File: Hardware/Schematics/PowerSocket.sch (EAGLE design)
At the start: 30 parts, among them IC1 ACS712-LC, T1 BT138-V, T2 BT138-V

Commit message: Updated schematic to use for a 3 slot device.
Some routing still remaining.
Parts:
- removed U$1: HLK-PM03, PowerSocket:HLK-PM03
- added ACOUT-NULL1, ACOUT-NULL2, ACOUT-PHASE1, ACOUT-PHASE2: -, wirepad:3,81/1,4
- added BUTTON_LED+1, BUTTON_LED+2, BUTTON_LED-1, BUTTON_LED-2, BUTTON_SWITCH3, BUTTON_SWITCH4, BUTTON_SWITCH5, BUTTON_SWITCH6: -, wirepad:2,15/1,0
- added C5, C7: 100nF, rcl:C-EUC1206
- added C6, C8: 470nF, rcl:C-EUC1206
- added D1: 1N4004, diode:1N4004
- added IC2, IC3: ACS712-LC, allegro-2:ACS712-LC
- added OK3, OK4, OK5, OK6: MOC3041S, optocoupler:MOC3041S
- added R11: 10K, rcl:R-TRIMM3296W
- added R12, R13, R14, R15, R16, R17, R18, R19: 150, eagle-ltspice:RR2010
- added R20, R22: 100, eagle-ltspice:RR2010
- added R21, R23: 10K, eagle-ltspice:RR2010
- added R5: 0, eagle-ltspice:RR2010
- added R6: 1M, rcl:R-TRIMM3296W
- added SUPPLY_3.3: 3.3V, wirepad:2,15/1,0
- added SUPPLY_GND: GND, wirepad:2,15/1,0
- added T3, T4, T5, T6: BT138-V, triac:BT138-V
- C3: device rcl:C-EUC1210 -> rcl:C-EU025-024X044
- OK1, OK2: value MOC3041M -> MOC3041S; device optocoupler:MOC3041M -> optocoupler:MOC3041S
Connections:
- removed net N$9 (its old number): ACIN-PHASE.P, T2.A1, U$1.AC1
- new net N$14: ACOUT-NULL1.P, R13.2, T3.A2
- new net N$16: BUTTON_LED+1.P, R20.2
- new net N$24: D1.A, R6.S
- new net N$25: R12.1, R14.2, U$2.IO12
- new net N$26: C6.2, IC2.FILTER
- new net N$27: IC2.VOUT, U$2.IO35
- new net N$28: OK3.C, R12.2
- new net N$29: OK3.A2, R13.1
- new net N$3: R11.S, R6.E, U$2.IO26
- new net N$30: OK3.A1, T3.G
- new net N$31: BUTTON_LED-1.P, U$2.IO23
- new net N$32: OK4.C, R14.1
- new net N$33: OK4.A2, R15.1
- new net N$34: OK4.A1, T4.G
- new net N$35: IC2.IP+, IC2.IP+1, R15.2, T4.A2
- new net N$36: ACOUT-PHASE1.P, IC2.IP-, IC2.IP-1
- new net N$37: BUTTON_LED+2.P, R22.2
- new net N$38: ACOUT-NULL2.P, R17.2, T5.A2
- new net N$39: BUTTON_SWITCH5.P, R23.2, U$2.IO17
- new net N$40: C8.2, IC3.FILTER
- new net N$41: IC3.VOUT, U$2.IO32
- new net N$42: OK5.C, R16.2
- new net N$43: OK5.A2, R17.1
- new net N$44: OK5.A1, T5.G
- new net N$45: ACIN-NULL.P, R5.1, T1.A1, T3.A1, T5.A1
- new net N$46: OK6.C, R18.1
- new net N$47: OK6.A2, R19.1
- new net N$48: OK6.A1, T6.G
- new net N$49: IC3.IP+, IC3.IP+1, R19.2, T6.A2
- new net N$50: ACOUT-PHASE2.P, IC3.IP-, IC3.IP-1
- new net N$51: ACIN-PHASE.P, D1.C, T2.A1, T4.A1, T6.A1
- new net N$52: BUTTON_LED-2.P, U$2.IO5
- new net N$54: R16.1, R18.2, U$2.IO14
- net GND: now also C5.2, C6.1, C7.2, C8.1, IC2.GND, IC3.GND, R11.E, R21.1, R23.1, R5.2, SUPPLY_GND.P; no longer U$1.-VO
- net N$17: now also U$2.IO19; no longer U$2.IO23
- net N$20: now also BUTTON_SWITCH3.P, R21.2, U$2.IO18; no longer ACIN-NULL.P, T1.A1, U$1.AC2
- net N$8: now also U$2.IO13; no longer U$2.IO17
- net VCC: now also BUTTON_SWITCH4.P, BUTTON_SWITCH6.P, C5.1, C7.1, IC2.VCC, IC3.VCC, OK3.A, OK4.A, OK5.A, OK6.A, R20.1, R22.1, SUPPLY_3.3.P; no longer U$1.+VO
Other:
- moved on the sheet: ACOUT-NULL, BUTTON_LED+, BUTTON_LED-, BUTTON_SWITCH1, BUTTON_SWITCH2, OK1, R3, R4, R7, R8, T1

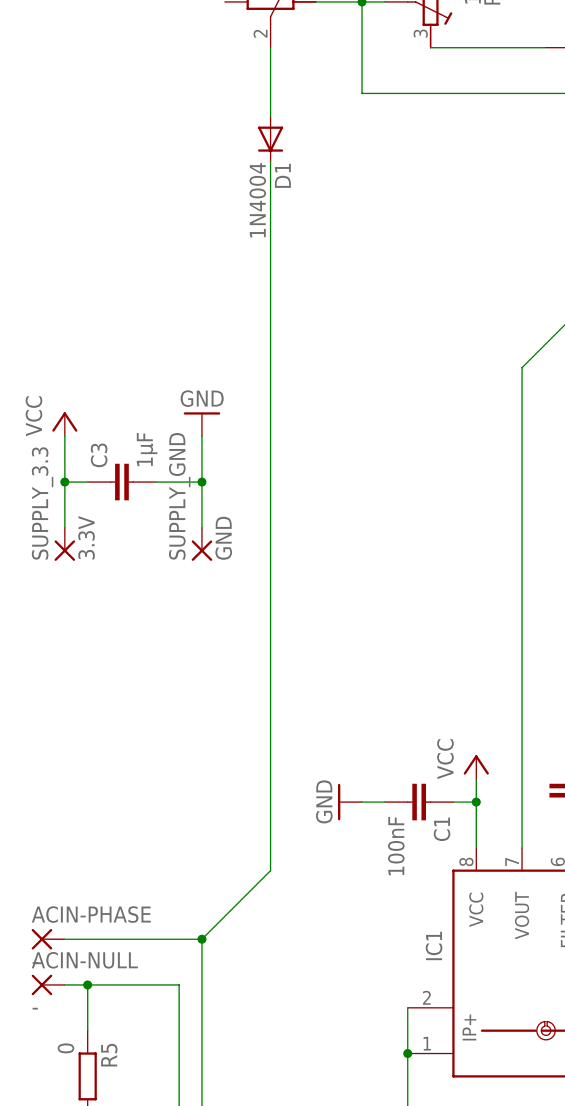
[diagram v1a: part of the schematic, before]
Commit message: Changed dimension to 50mmx100mm and routed the board
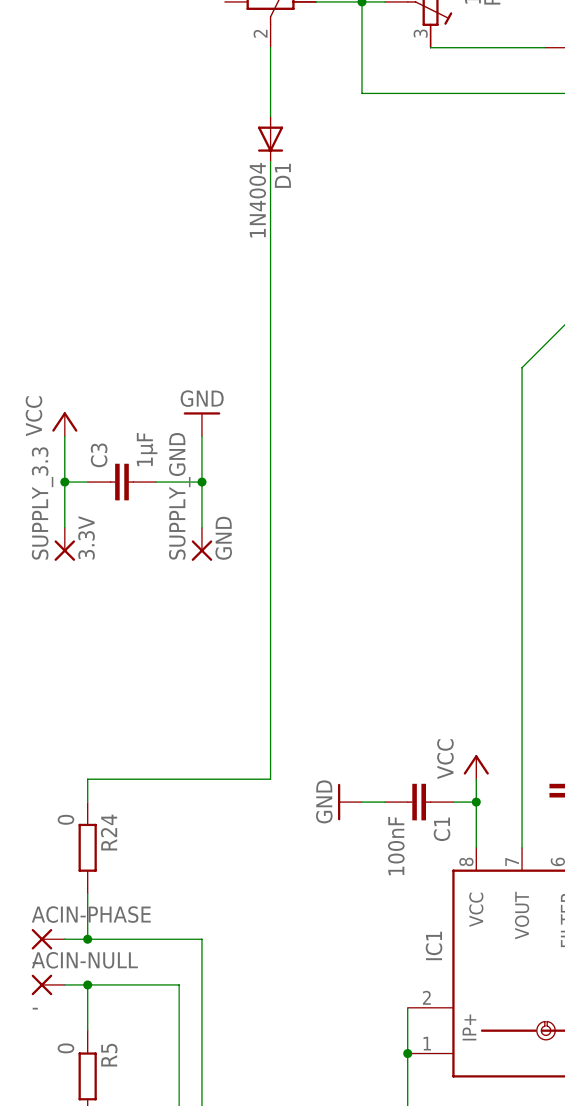
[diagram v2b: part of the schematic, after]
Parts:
- added R24: 0, eagle-ltspice:RR2010
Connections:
- new net N$53: D1.C, R24.1
- net N$51: now also R24.2; no longer D1.C
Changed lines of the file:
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@@
 <?xml version="1.0" encoding="utf-8"?>
 <!DOCTYPE eagle SYSTEM "eagle.dtd">
-<eagle version="7.6.0">
+<eagle version="6.6.0">
 <drawing>
 <settings>
@@
 <part name="GND19" library="supply1" deviceset="GND" device=""/>
 <part name="P+20" library="supply1" deviceset="VCC" device=""/>
+<part name="R24" library="eagle-ltspice" deviceset="R" device="R2010" value="0"/>
 </parts>
 <sheets>
@@
 <instance part="GND19" gate="1" x="292.1" y="266.7" rot="R180"/>
 <instance part="P+20" gate="VCC" x="299.72" y="269.24"/>
+<instance part="R24" gate="G$1" x="48.26" y="76.2" rot="R270"/>
 </instances>
 <busses>
@@
 <wire x1="241.3" y1="30.48" x2="241.3" y2="10.16" width="0.1524" layer="91"/>
 <pinref part="ACIN-PHASE" gate="1" pin="P"/>
-<wire x1="60.96" y1="66.04" x2="45.72" y2="66.04" width="0.1524" layer="91"/>
+<wire x1="60.96" y1="66.04" x2="48.26" y2="66.04" width="0.1524" layer="91"/>
+<wire x1="48.26" y1="66.04" x2="45.72" y2="66.04" width="0.1524" layer="91"/>
 <wire x1="60.96" y1="66.04" x2="60.96" y2="33.02" width="0.1524" layer="91"/>
 <pinref part="T2" gate="G$1" pin="A1"/>
 <wire x1="60.96" y1="33.02" x2="162.56" y2="33.02" width="0.1524" layer="91"/>
 <wire x1="162.56" y1="33.02" x2="162.56" y2="45.72" width="0.1524" layer="91"/>
-<wire x1="60.96" y1="66.04" x2="68.58" y2="73.66" width="0.1524" layer="91"/>
-<pinref part="D1" gate="1" pin="C"/>
-<wire x1="68.58" y1="73.66" x2="68.58" y2="152.4" width="0.1524" layer="91"/>
 <wire x1="241.3" y1="10.16" x2="162.56" y2="10.16" width="0.1524" layer="91"/>
 <wire x1="162.56" y1="10.16" x2="162.56" y2="33.02" width="0.1524" layer="91"/>
@@
 <wire x1="370.84" y1="15.24" x2="370.84" y2="30.48" width="0.1524" layer="91"/>
 <junction x="370.84" y="30.48"/>
-<junction x="60.96" y="66.04"/>
+<pinref part="R24" gate="G$1" pin="2"/>
+<wire x1="48.26" y1="66.04" x2="48.26" y2="71.12" width="0.1524" layer="91"/>
+<junction x="48.26" y="66.04"/>
 </segment>
 </net>
@@
 </segment>
 </net>
+<net name="N$53" class="0">
+<segment>
+<pinref part="R24" gate="G$1" pin="1"/>
+<wire x1="48.26" y1="81.28" x2="48.26" y2="83.82" width="0.1524" layer="91"/>
+<pinref part="D1" gate="1" pin="C"/>
+<wire x1="48.26" y1="83.82" x2="68.58" y2="83.82" width="0.1524" layer="91"/>
+<wire x1="68.58" y1="83.82" x2="68.58" y2="152.4" width="0.1524" layer="91"/>
+</segment>
+</net>

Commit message: Schematic changes: Added JTAG pins. Changed some resistors to 0805 type. Only use 3 holes for the buttons. Changed current sensor to 3.3V tolerant ACS710. Some rewiring needed on board.
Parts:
- removed BUTTON_SWITCH2, BUTTON_SWITCH4, BUTTON_SWITCH6: -, wirepad:2,15/1,0
- removed C7: 100nF, rcl:C-EUC1206
- removed C8: 470nF, rcl:C-EUC1206
- removed IC1, IC2, IC3: ACS712-LC, allegro-2:ACS712-LC
- removed R24: 0, eagle-ltspice:RR2010
- added C10: 1nF, rcl:C-EUC1206
- added C11, C12, C13: 100nF, rcl:C-EUC1206
- added C9: 470nF, rcl:C-EUC1206
- added JTAG: -, pinhead:PINHD-1X4
- added U$1, U$3, U$4: ACS710, PowerSocket:ACS710
- BUTTON_LED+: value - -> BUTTON_VCC
- C1, C5: value 100nF -> 470nF
- C4, C6: value 470nF -> 1nF
- R1, R12, R16, R2, R20, R21, R22, R23, R3, R7, R8: device eagle-ltspice:RR2010 -> rcl:R-EU_R0805
- R11: device rcl:R-TRIMM3296W -> rcl:R-EU_R0805
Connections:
- removed net N$27: IC2.VOUT, U$2.IO35
- removed net N$37: BUTTON_LED+2.P, R22.2
- removed net N$40: C8.2, IC3.FILTER
- removed net N$50: ACOUT-PHASE2.P, IC3.IP-, IC3.IP-1
- new net N$55: C9.2, U$1.FILTER
- new net N$56: JTAG.4, U$2.IO14
- new net N$57: JTAG.3, U$2.IO12
- new net N$58: JTAG.2, U$2.IO13
- new net N$59: JTAG.1, U$2.IO15
- new net N$60: C10.2, U$1.VZCR
- new net N$61: U$3.IP-, U$3.IP-1, U$3.IP-2, U$3.IP-3
- new net N$62: C1.2, U$3.FILTER
- new net N$63: C4.2, U$3.VZCR
- new net N$64: C5.2, U$4.FILTER
- new net N$65: C6.2, U$4.VZCR
- net GND: now also C1.1, C10.1, C11.1, C12.1, C13.1, C5.1, C9.1, R11.2, U$1.FAULT_EN, U$1.GND, U$3.FAULT_EN, U$3.GND, U$4.FAULT_EN, U$4.GND; no longer C1.2, C5.2, C7.2, C8.1, IC1.GND, IC2.GND, IC3.GND, R11.E
- net N$11: now also U$2.IO35, U$3.VIOUT; no longer C4.2, IC1.FILTER
- net N$12: now also U$1.VIOUT; no longer IC1.VOUT
- net N$13: now also U$1.IP-, U$1.IP-1, U$1.IP-2, U$1.IP-3; no longer IC1.IP-, IC1.IP-1
- net N$15: now also BUTTON_LED-.P, R7.1; no longer BUTTON_LED+.P, R7.2
- net N$16: now also BUTTON_LED-1.P, R20.1; no longer BUTTON_LED+1.P, R20.2
- net N$23: now also U$1.IP+, U$1.IP+1, U$1.IP+2, U$1.IP+3; no longer IC1.IP+, IC1.IP+1
- net N$25: now also U$2.IO26; no longer U$2.IO12
- net N$26: now also BUTTON_LED-2.P, R22.1; no longer C6.2, IC2.FILTER
- net N$3: now also R11.1, U$2.IO33; no longer R11.S, U$2.IO26
- net N$31: now also R20.2; no longer BUTTON_LED-1.P
- net N$35: now also U$4.IP-, U$4.IP-1, U$4.IP-2, U$4.IP-3; no longer IC2.IP+, IC2.IP+1, R15.2, T4.A2
- net N$36: no longer IC2.IP-, IC2.IP-1
- net N$41: now also U$4.VIOUT; no longer IC3.VOUT
- net N$49: now also U$4.IP+, U$4.IP+1, U$4.IP+2, U$4.IP+3; no longer IC3.IP+, IC3.IP+1
- net N$51: now also D1.C; no longer R24.2
- net N$52: now also R22.2; no longer BUTTON_LED-2.P
- net N$53: now also R15.2, T4.A2, U$3.IP+, U$3.IP+1, U$3.IP+2, U$3.IP+3; no longer D1.C, R24.1
- net N$54: now also U$2.IO27; no longer U$2.IO14
- net N$8: now also U$2.IO25; no longer U$2.IO13
- net N$9: now also R7.2; no longer BUTTON_LED-.P
- net VCC: now also BUTTON_LED+.P, BUTTON_LED+1.P, BUTTON_LED+2.P, C11.2, C12.2, C13.2, U$1.VCC, U$1.VOC, U$3.VCC, U$3.VOC, U$4.VCC, U$4.VOC; no longer BUTTON_SWITCH2.P, BUTTON_SWITCH4.P, BUTTON_SWITCH6.P, C1.1, C5.1, C7.1, IC1.VCC, IC2.VCC, IC3.VCC, R20.1, R22.1, R7.1
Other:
- moved on the sheet: ACOUT-PHASE, BUTTON_LED-, BUTTON_LED-1, BUTTON_LED-2, C1, C4, C5, C6, R20, R22, R7, R8

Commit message: Did some routing of the board.
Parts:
- C1, C10, C11, C12, C13, C4, C5, C6, C9: device rcl:C-EUC1206 -> rcl:C-EUC0805
- R14, R18: device eagle-ltspice:RR2010 -> rcl:C-EUC0805
- R9: device eagle-ltspice:RR2010 -> rcl:R-EU_R0805
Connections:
- removed net N$61: U$3.IP-, U$3.IP-1, U$3.IP-2, U$3.IP-3
- new net N$27: U$1.NFAULT
- new net N$40: U$3.NFAULT
- new net N$50: U$4.NFAULT
- net N$35: now also ACOUT-PHASE2.P
- net N$36: now also U$3.IP-, U$3.IP-1, U$3.IP-2, U$3.IP-3
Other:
- moved on the sheet: ACOUT-PHASE, ACOUT-PHASE1, ACOUT-PHASE2, R14, R18

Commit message: Routed board.
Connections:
- net N$3: now also U$2.IO4; no longer U$2.IO33
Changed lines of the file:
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@@
 <grid distance="0.1" unitdist="inch" unit="inch" style="lines" multiple="1" display="no" altdistance="0.01" altunitdist="inch" altunit="inch"/>
 <layers>
-<layer number="1" name="Top" color="4" fill="1" visible="yes" active="no"/>
-<layer number="16" name="Bottom" color="1" fill="1" visible="yes" active="no"/>
-<layer number="17" name="Pads" color="2" fill="1" visible="yes" active="no"/>
-<layer number="18" name="Vias" color="2" fill="1" visible="yes" active="no"/>
-<layer number="19" name="Unrouted" color="6" fill="1" visible="yes" active="no"/>
-<layer number="20" name="Dimension" color="15" fill="1" visible="yes" active="no"/>
-<layer number="21" name="tPlace" color="7" fill="1" visible="yes" active="no"/>
-<layer number="22" name="bPlace" color="7" fill="1" visible="yes" active="no"/>
-<layer number="23" name="tOrigins" color="15" fill="1" visible="yes" active="no"/>
-<layer number="24" name="bOrigins" color="15" fill="1" visible="yes" active="no"/>
-<layer number="25" name="tNames" color="7" fill="1" visible="yes" active="no"/>
-<layer number="26" name="bNames" color="7" fill="1" visible="yes" active="no"/>
-<layer number="27" name="tValues" color="7" fill="1" visible="yes" active="no"/>
-<layer number="28" name="bValues" color="7" fill="1" visible="yes" active="no"/>
+<layer number="1" name="Top" color="4" fill="1" visible="no" active="no"/>
+<layer number="16" name="Bottom" color="1" fill="1" visible="no" active="no"/>
+<layer number="17" name="Pads" color="2" fill="1" visible="no" active="no"/>
+<layer number="18" name="Vias" color="2" fill="1" visible="no" active="no"/>
+<layer number="19" name="Unrouted" color="6" fill="1" visible="no" active="no"/>
+<layer number="20" name="Dimension" color="15" fill="1" visible="no" active="no"/>
+<layer number="21" name="tPlace" color="7" fill="1" visible="no" active="no"/>
+<layer number="22" name="bPlace" color="7" fill="1" visible="no" active="no"/>
+<layer number="23" name="tOrigins" color="15" fill="1" visible="no" active="no"/>
+<layer number="24" name="bOrigins" color="15" fill="1" visible="no" active="no"/>
+<layer number="25" name="tNames" color="7" fill="1" visible="no" active="no"/>
+<layer number="26" name="bNames" color="7" fill="1" visible="no" active="no"/>
+<layer number="27" name="tValues" color="7" fill="1" visible="no" active="no"/>
+<layer number="28" name="bValues" color="7" fill="1" visible="no" active="no"/>
 <layer number="29" name="tStop" color="7" fill="3" visible="no" active="no"/>
 <layer number="30" name="bStop" color="7" fill="6" visible="no" active="no"/>
@@
 <layer number="35" name="tGlue" color="7" fill="4" visible="no" active="no"/>
 <layer number="36" name="bGlue" color="7" fill="5" visible="no" active="no"/>
-<layer number="37" name="tTest" color="7" fill="1" visible="yes" active="no"/>
-<layer number="38" name="bTest" color="7" fill="1" visible="yes" active="no"/>
+<layer number="37" name="tTest" color="7" fill="1" visible="no" active="no"/>
+<layer number="38" name="bTest" color="7" fill="1" visible="no" active="no"/>
 <layer number="39" name="tKeepout" color="4" fill="11" visible="no" active="no"/>
 <layer number="40" name="bKeepout" color="1" fill="11" visible="no" active="no"/>
@@
 <layer number="44" name="Drills" color="7" fill="1" visible="no" active="no"/>
 <layer number="45" name="Holes" color="7" fill="1" visible="no" active="no"/>
-<layer number="46" name="Milling" color="3" fill="1" visible="yes" active="no"/>
-<layer number="47" name="Measures" color="7" fill="1" visible="yes" active="no"/>
-<layer number="48" name="Document" color="7" fill="1" visible="yes" active="no"/>
-<layer number="49" name="Reference" color="7" fill="1" visible="yes" active="no"/>
-<layer number="50" name="dxf" color="7" fill="1" visible="yes" active="no"/>
-<layer number="51" name="tDocu" color="7" fill="1" visible="yes" active="no"/>
-<layer number="52" name="bDocu" color="7" fill="1" visible="yes" active="no"/>
-<layer number="56" name="wert" color="7" fill="1" visible="yes" active="no"/>
+<layer number="46" name="Milling" color="3" fill="1" visible="no" active="no"/>
+<layer number="47" name="Measures" color="7" fill="1" visible="no" active="no"/>
+<layer number="48" name="Document" color="7" fill="1" visible="no" active="no"/>
+<layer number="49" name="Reference" color="7" fill="1" visible="no" active="no"/>
+<layer number="50" name="dxf" color="7" fill="1" visible="no" active="no"/>
+<layer number="51" name="tDocu" color="7" fill="1" visible="no" active="no"/>
+<layer number="52" name="bDocu" color="7" fill="1" visible="no" active="no"/>
+<layer number="56" name="wert" color="7" fill="1" visible="no" active="no"/>
 <layer number="90" name="Modules" color="5" fill="1" visible="yes" active="yes"/>
 <layer number="91" name="Nets" color="2" fill="1" visible="yes" active="yes"/>
@@
 <pinref part="R6" gate="G$1" pin="E"/>
 <wire x1="78.74" y1="170.18" x2="73.66" y2="170.18" width="0.1524" layer="91"/>
-<wire x1="78.74" y1="160.02" x2="78.74" y2="170.18" width="0.1524" layer="91"/>
-<pinref part="U$2" gate="G$1" pin="IO33"/>
-<wire x1="137.16" y1="165.1" x2="106.68" y2="165.1" width="0.1524" layer="91"/>
-<wire x1="106.68" y1="165.1" x2="106.68" y2="160.02" width="0.1524" layer="91"/>
-<wire x1="106.68" y1="160.02" x2="78.74" y2="160.02" width="0.1524" layer="91"/>
 <pinref part="R11" gate="G$1" pin="1"/>
 <wire x1="78.74" y1="175.26" x2="78.74" y2="170.18" width="0.1524" layer="91"/>
 <junction x="78.74" y="170.18"/>
-</segment>
-</net>
+<wire x1="78.74" y1="170.18" x2="78.74" y2="124.46" width="0.1524" layer="91"/>
+<wire x1="78.74" y1="124.46" x2="162.56" y2="124.46" width="0.1524" layer="91"/>
+<wire x1="162.56" y1="124.46" x2="162.56" y2="127" width="0.1524" layer="91"/>
+<wire x1="162.56" y1="127" x2="170.18" y2="127" width="0.1524" layer="91"/>
+<wire x1="170.18" y1="127" x2="170.18" y2="137.16" width="0.1524" layer="91"/>
+<pinref part="U$2" gate="G$1" pin="IO4"/>
+<wire x1="170.18" y1="137.16" x2="167.64" y2="137.16" width="0.1524" layer="91"/>
+<wire x1="167.64" y1="137.16" x2="167.64" y2="142.24" width="0.1524" layer="91"/>
+</segment>
+</net>
